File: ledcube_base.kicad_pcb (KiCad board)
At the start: 2 copper layers, 100 x 100 mm, 33 parts, among them CON1 BARREL_JACK, P1 CONN_02X02, P10 CONN_02X02, P11 CONN_02X02, P12 CONN_02X02, P13 CONN_02X02, P14 CONN_02X02, P15 CONN_02X02, P16 CONN_02X02, P17 CONN_02X02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

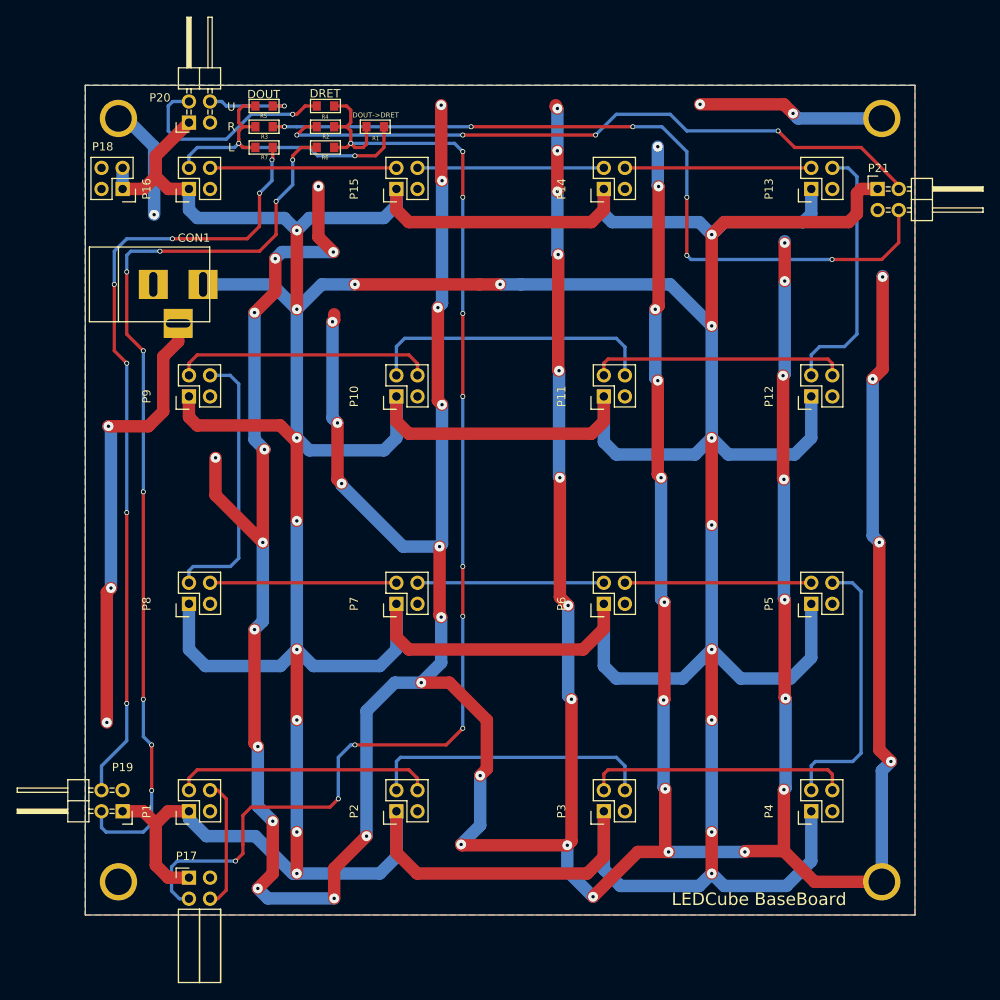
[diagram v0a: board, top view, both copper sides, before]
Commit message: Fixed: Via Drill Size
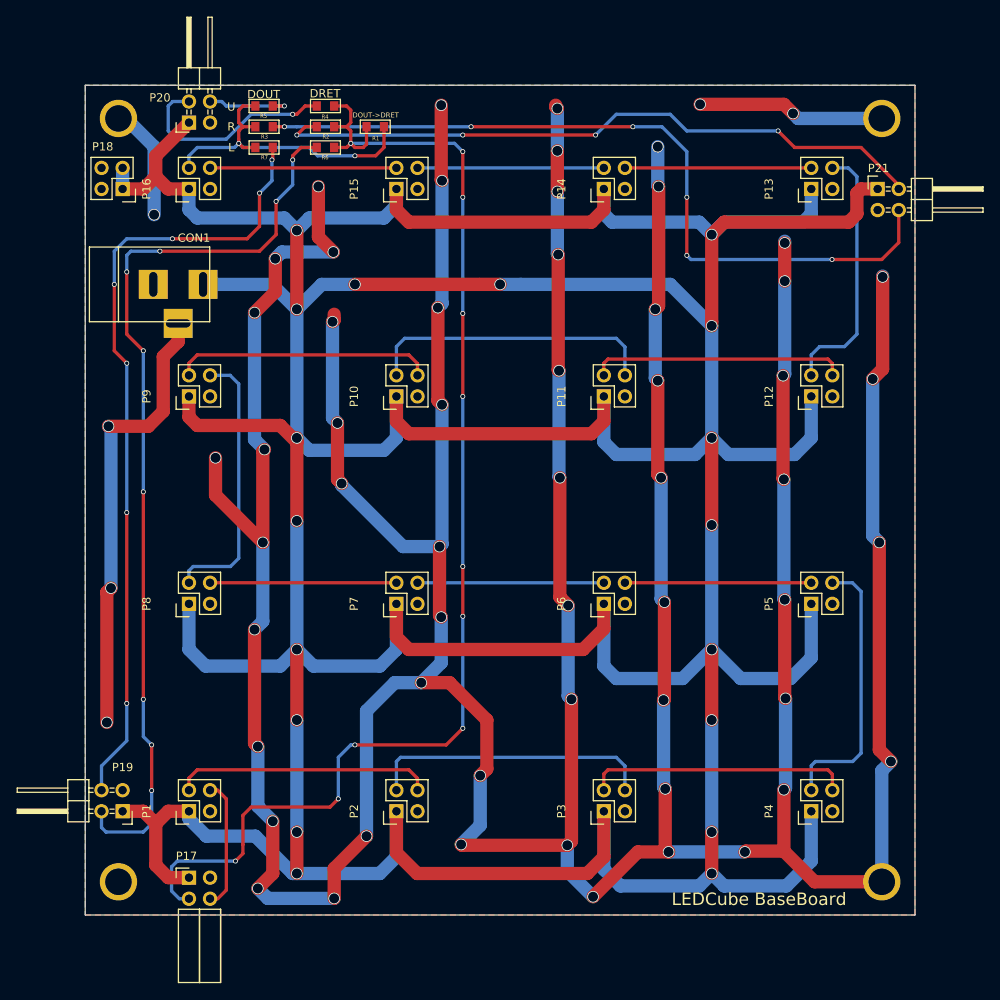
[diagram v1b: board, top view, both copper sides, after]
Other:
- net class Supply: trace_width 1.5 -> 1.6; via_dia 1.2 -> 1.4; via_drill 0.4 -> 1.2
